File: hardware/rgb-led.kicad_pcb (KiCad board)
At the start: 2 copper layers, 17.5 x 25 mm, 19 parts, among them P1 CON-SENSOR, Q1 2N7002P, U1 M24C64, U2 DRILL, U3 DRILL, U4 DRILL, U5 DRILL

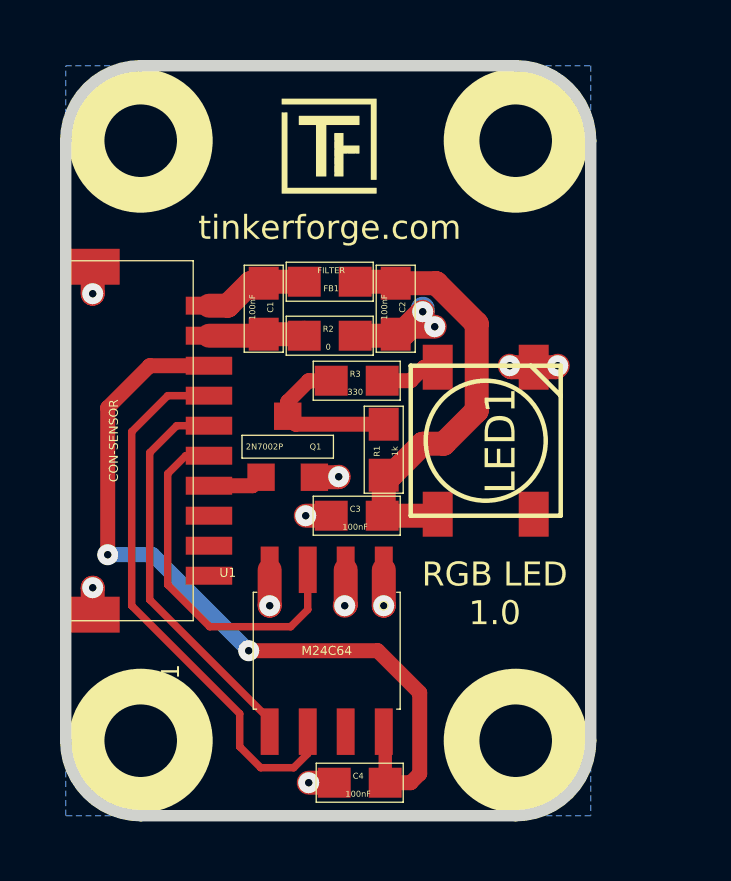
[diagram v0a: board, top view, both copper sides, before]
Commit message: add fiducials
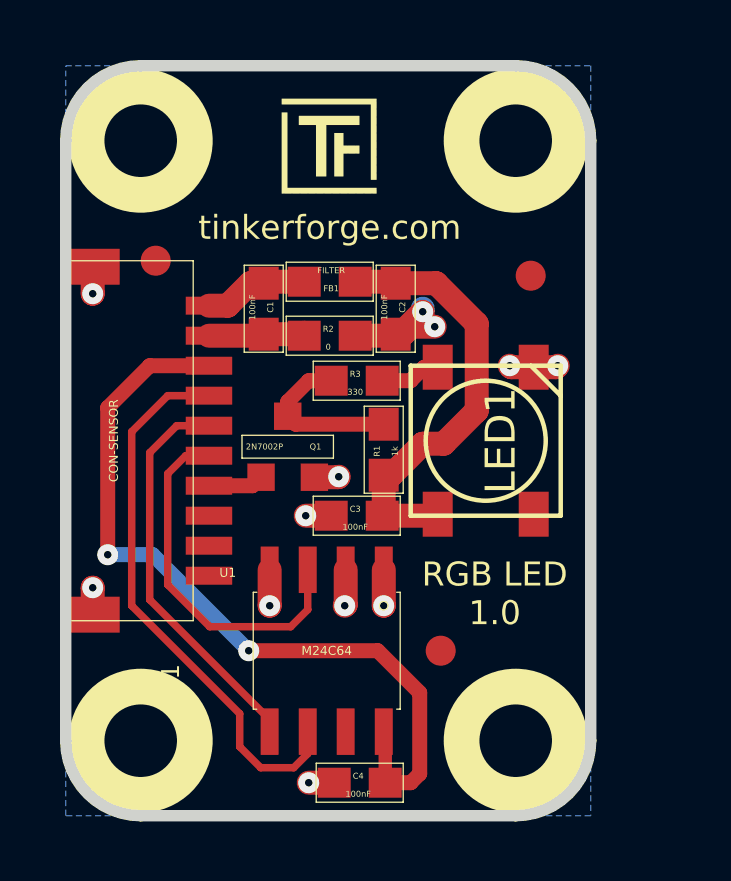
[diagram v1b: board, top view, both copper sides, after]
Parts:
- added Fiducial_Mark: VAL**, kicad-libraries:Fiducial_Mark, F.Cu at (140.8, 112.6)
- added Fiducial_Mark: VAL**, kicad-libraries:Fiducial_Mark, F.Cu at (137.8, 125.1)
- added Fiducial_Mark: VAL**, kicad-libraries:Fiducial_Mark, F.Cu at (128.3, 112.1)
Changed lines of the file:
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@@
-(kicad_pcb (version 4) (host pcbnew "(2015-03-18 BZR 5525)-product")
+(kicad_pcb (version 4) (host pcbnew 4.0.2-4+6225~38~ubuntu15.10.1-stable)
   (general
     (links 27)
@@
     (tracks 107)
     (zones 0)
-    (modules 19)
+    (modules 22)
     (nets 12)
   )
@@
     (pad_drill 1.30048)
     (pad_to_mask_clearance 0)
-    (aux_axis_origin 125.30074 118.09984)
+    (aux_axis_origin 125.3 105.6)
+    (grid_origin 125.3 105.6)
     (visible_elements FFFFFF9F)
     (pcbplotparams
@@
       (xy 2.3114 -1.41732) (xy 2.3114 -1.67132) (xy 2.3114 -1.67132)) (layer B.SilkS) (width 0.00254))
   )
+  (module kicad-libraries:Fiducial_Mark (layer Vorderseite)
+    (at 140.8 112.6)
+    (attr smd)
+    (fp_text reference Fiducial_Mark (at 0 0) (layer F.SilkS) hide
+      (effects (font (size 0.127 0.127) (thickness 0.03302)))
+    )
+    (fp_text value VAL** (at 0 -0.29972) (layer F.SilkS) hide
+      (effects (font (size 0.127 0.127) (thickness 0.03302)))
+    )
+    (fp_circle (center 0 0) (end 1.15062 0) (layer Dwgs.User) (width 0.01016))
+    (pad 1 smd circle (at 0 0) (size 1.00076 1.00076) (layers Vorderseite F.Paste F.Mask)
+      (clearance 0.65024))
+  )
+  (module kicad-libraries:Fiducial_Mark (layer Vorderseite)
+    (at 137.8 125.1)
+    (attr smd)
+    (fp_text reference Fiducial_Mark (at 0 0) (layer F.SilkS) hide
+      (effects (font (size 0.127 0.127) (thickness 0.03302)))
+    )
+    (fp_text value VAL** (at 0 -0.29972) (layer F.SilkS) hide
+      (effects (font (size 0.127 0.127) (thickness 0.03302)))
+    )
+    (fp_circle (center 0 0) (end 1.15062 0) (layer Dwgs.User) (width 0.01016))
+    (pad 1 smd circle (at 0 0) (size 1.00076 1.00076) (layers Vorderseite F.Paste F.Mask)
+      (clearance 0.65024))
+  )
+  (module kicad-libraries:Fiducial_Mark (layer Vorderseite)
+    (at 128.3 112.1)
+    (attr smd)
+    (fp_text reference Fiducial_Mark (at 0 0) (layer F.SilkS) hide
+      (effects (font (size 0.127 0.127) (thickness 0.03302)))
+    )
+    (fp_text value VAL** (at 0 -0.29972) (layer F.SilkS) hide
+      (effects (font (size 0.127 0.127) (thickness 0.03302)))
+    )
+    (fp_circle (center 0 0) (end 1.15062 0) (layer Dwgs.User) (width 0.01016))
+    (pad 1 smd circle (at 0 0) (size 1.00076 1.00076) (layers Vorderseite F.Paste F.Mask)
+      (clearance 0.65024))
+  )
   (gr_line (start 125.3 108.1) (end 125.3 128.1) (angle 90) (layer Edge.Cuts) (width 0.381))

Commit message: fix rgb led bricklets dimensions
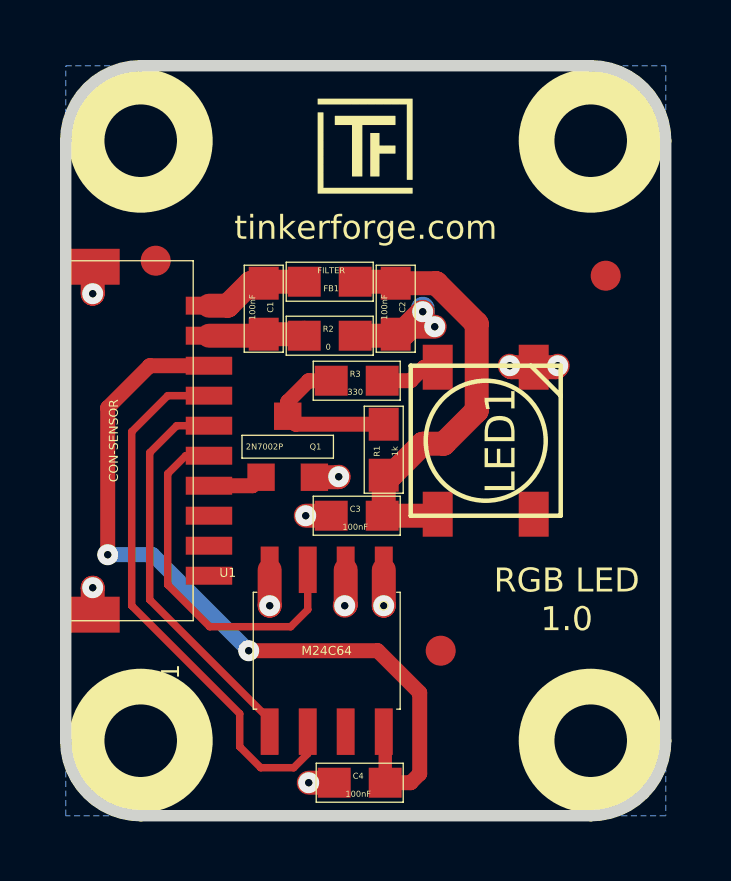
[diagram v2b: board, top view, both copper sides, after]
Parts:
- moved VAL 3.00 mm to (140.3, 118.2)
- moved Fiducial_Mark 2.50 mm to (143.3, 112.6)
- moved U3 2.50 mm to (142.8, 128.1)
- moved U5 2.50 mm to (142.8, 108.1)
- moved G*** 1.20 mm to (133.7, 106.7)
- moved G*** 0.10 mm to (130.3, 118.2)
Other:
- board size 17.5 x 25 mm -> 20 x 25 mm
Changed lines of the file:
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@@
-(kicad_pcb (version 4) (host pcbnew 4.0.2-4+6225~38~ubuntu15.10.1-stable)
+(kicad_pcb (version 4) (host pcbnew 4.0.2+e4-6225~38~ubuntu15.10.1-stable)
   (general
     (links 27)
@@
   )
   (module kicad-libraries:DRILL_NP (layer Vorderseite)
-    (at 140.3 128.1 90)
+    (at 142.8 128.1 90)
     (fp_text reference U3 (at 0 0 90) (layer F.SilkS) hide
       (effects (font (size 0.29972 0.29972) (thickness 0.0762)))
@@
   )
   (module kicad-libraries:DRILL_NP (layer Vorderseite)
-    (at 140.3 108.1)
+    (at 142.8 108.1)
     (clearance 0.89916)
     (fp_text reference U5 (at 0 0) (layer F.SilkS) hide
@@
   )
   (module kicad-libraries:Logo_31x31 (layer Vorderseite)
-    (at 132.5 106.7)
+    (at 133.7 106.7)
     (fp_text reference G*** (at 1.34874 2.97434) (layer F.SilkS) hide
       (effects (font (size 0.29972 0.29972) (thickness 0.0762)))
@@
   )
   (module kicad-libraries:WEEE_7mm (layer Rückseite)
-    (at 130.3 118.1 180)
+    (at 130.3 118.2 180)
     (fp_text reference G*** (at 0 0 180) (layer B.SilkS) hide
       (effects (font (thickness 0.3)) (justify mirror))
@@
   )
   (module kicad-libraries:CE_5mm (layer Rückseite)
-    (at 137.3 118.1 180)
+    (at 140.3 118.2 180)
     (fp_text reference VAL (at 0 0 180) (layer B.SilkS) hide
       (effects (font (size 1.143 1.143) (thickness 0.1778)) (justify mirror))
@@
   )
   (module kicad-libraries:Fiducial_Mark (layer Vorderseite)
-    (at 140.8 112.6)
+    (at 143.3 112.6)
     (attr smd)
     (fp_text reference Fiducial_Mark (at 0 0) (layer F.SilkS) hide
@@
       (clearance 0.65024))
   )
+  (gr_line (start 127.8 130.6) (end 142.8 130.6) (angle 90) (layer Edge.Cuts) (width 0.381))
+  (gr_line (start 142.8 105.6) (end 127.8 105.6) (angle 90) (layer Edge.Cuts) (width 0.381))
   (gr_line (start 125.3 108.1) (end 125.3 128.1) (angle 90) (layer Edge.Cuts) (width 0.381))
-  (gr_line (start 140.3 105.6) (end 127.8 105.6) (angle 90) (layer Edge.Cuts) (width 0.381))
-  (gr_line (start 142.8 128.1) (end 142.8 108.1) (angle 90) (layer Edge.Cuts) (width 0.381))
-  (gr_line (start 127.8 130.6) (end 140.3 130.6) (angle 90) (layer Edge.Cuts) (width 0.381))
+  (gr_line (start 145.3 128.1) (end 145.3 108.1) (angle 90) (layer Edge.Cuts) (width 0.381))
   (gr_arc (start 127.8 128.1) (end 127.8 130.6) (angle 90) (layer Edge.Cuts) (width 0.381))
-  (gr_arc (start 140.3 128.1) (end 142.8 128.1) (angle 90) (layer Edge.Cuts) (width 0.381))
-  (gr_arc (start 140.3 108.1) (end 140.3 105.6) (angle 90) (layer Edge.Cuts) (width 0.381))
+  (gr_arc (start 142.8 128.1) (end 145.3 128.1) (angle 90) (layer Edge.Cuts) (width 0.381))
+  (gr_arc (start 142.8 108.1) (end 142.8 105.6) (angle 90) (layer Edge.Cuts) (width 0.381))
   (gr_arc (start 127.8 108.1) (end 125.3 108.1) (angle 90) (layer Edge.Cuts) (width 0.381))
   (gr_text "Copyright Tinkerforge GmbH 2015.\nThis documentation describes Open Hardware and is licensed under the\nCERN OHL v. 1.1.\nYou may redistribute and modify this documentation under the terms of the\nCERN OHL v.1.1. (http://ohwr.org/cernohl). This documentation is distributed\nWITHOUT ANY EXPRESS OR IMPLIED WARRANTY, INCLUDING OF\nMERCHANTABILITY, SATISFACTORY QUALITY AND FITNESS FOR A\nPARTICULAR PURPOSE. Please see the CERN OHL v.1.1 for applicable\nconditions" (at 258.8 156.55) (layer Cmts.User)
     (effects (font (size 0.8001 0.8001) (thickness 0.200025) italic))
   )
-  (gr_text tinkerforge.com (at 134.1 111) (layer F.SilkS)
+  (gr_text tinkerforge.com (at 135.3 111) (layer F.SilkS)
     (effects (font (size 0.8001 0.8001) (thickness 0.14986)))
   )
-  (gr_text "RGB LED\n1.0" (at 139.6 123.2) (layer F.SilkS)
+  (gr_text "RGB LED\n1.0" (at 142 123.4) (layer F.SilkS)
     (effects (font (size 0.8001 0.8001) (thickness 0.14986)))
   )
@@
     (polygon
       (pts
-        (xy 125.3 105.6) (xy 142.8 105.6) (xy 142.8 130.6) (xy 125.3 130.6)
+        (xy 125.3 105.6) (xy 145.3 105.6) (xy 145.3 130.6) (xy 125.3 130.6)
       )
     )

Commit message: increase version number to 1.1
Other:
- board text added: "Copyright Tinkerforge GmbH 2016. This documentation describes Open Hardware and is licensed under the CERN OHL v. 1.1. You may redistribute and modify this documentation under the terms of the CERN OHL v.1.1. (http://ohwr.org/cernohl). This documentation is distributed WITHOUT ANY EXPRESS OR IMPLIED WARRANTY, INCLUDING OF MERCHANTABILITY, SATISFACTORY QUALITY AND FITNESS FOR A PARTICULAR PURPOSE.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"
- board text added: "RGB LED 1.1"
- board text removed: "Copyright Tinkerforge GmbH 2015. This documentation describes Open Hardware and is licensed under the CERN OHL v. 1.1. You may redistribute and modify this documentation under the terms of the CERN OHL v.1.1. (http://ohwr.org/cernohl). This documentation is distributed WITHOUT ANY EXPRESS OR IMPLIED WARRANTY, INCLUDING OF MERCHANTABILITY, SATISFACTORY QUALITY AND FITNESS FOR A PARTICULAR PURPOSE.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"
- board text removed: "RGB LED 1.0"
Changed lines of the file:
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@@
   (title_block
     (title "RGB LED Bricklet")
-    (date "Mi 18 Nov 2015")
-    (rev 1.0)
+    (date 2016-08-04)
+    (rev 1.1)
     (company "Tinkerforge GmbH")
     (comment 1 "Licensed under CERN OHL v.1.1")
-    (comment 2 "Copyright (©) 2015, B.Nordmeyer <bastian@tinkerforge.com>")
+    (comment 2 "Copyright (©) 2016, B.Nordmeyer <bastian@tinkerforge.com>")
   )
   (layers
@@
   (gr_arc (start 142.8 108.1) (end 142.8 105.6) (angle 90) (layer Edge.Cuts) (width 0.381))
   (gr_arc (start 127.8 108.1) (end 125.3 108.1) (angle 90) (layer Edge.Cuts) (width 0.381))
-  (gr_text "Copyright Tinkerforge GmbH 2015.\nThis documentation describes Open Hardware and is licensed under the\nCERN OHL v. 1.1.\nYou may redistribute and modify this documentation under the terms of the\nCERN OHL v.1.1. (http://ohwr.org/cernohl). This documentation is distributed\nWITHOUT ANY EXPRESS OR IMPLIED WARRANTY, INCLUDING OF\nMERCHANTABILITY, SATISFACTORY QUALITY AND FITNESS FOR A\nPARTICULAR PURPOSE. Please see the CERN OHL v.1.1 for applicable\nconditions" (at 258.8 156.55) (layer Cmts.User)
+  (gr_text "Copyright Tinkerforge GmbH 2016.\nThis documentation describes Open Hardware and is licensed under the\nCERN OHL v. 1.1.\nYou may redistribute and modify this documentation under the terms of the\nCERN OHL v.1.1. (http://ohwr.org/cernohl). This documentation is distributed\nWITHOUT ANY EXPRESS OR IMPLIED WARRANTY, INCLUDING OF\nMERCHANTABILITY, SATISFACTORY QUALITY AND FITNESS FOR A\nPARTICULAR PURPOSE. Please see the CERN OHL v.1.1 for applicable\nconditions" (at 258.8 156.55) (layer Cmts.User)
     (effects (font (size 0.8001 0.8001) (thickness 0.200025) italic))
   )
@@
     (effects (font (size 0.8001 0.8001) (thickness 0.14986)))
   )
-  (gr_text "RGB LED\n1.0" (at 142 123.4) (layer F.SilkS)
+  (gr_text "RGB LED\n1.1" (at 142 123.4) (layer F.SilkS)
     (effects (font (size 0.8001 0.8001) (thickness 0.14986)))
   )

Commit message: Add 3d information (final)
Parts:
- C1, C2, C3, C4, FB1: footprint kicad-libraries:0603E -> kicad-libraries:C0603E
- R1, R2, R3: footprint kicad-libraries:0603E -> kicad-libraries:R0603E
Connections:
- LED1 pad 2: (no net) -> Net-(LED1-Pad2)
- P1 pad 10: (no net) -> Net-(P1-Pad10)
- P1 pad 8: (no net) -> Net-(P1-Pad8)
- P1 pad 9: (no net) -> Net-(P1-Pad9)
- U1 pad 7: (no net) -> Net-(U1-Pad7)
